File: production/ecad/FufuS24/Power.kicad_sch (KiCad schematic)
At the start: 57 parts, among them U4 TPS785, U5 PLMR38020FDDAR, U6 PLMR38020FDDAR, U7 PLMR38020FDDAR

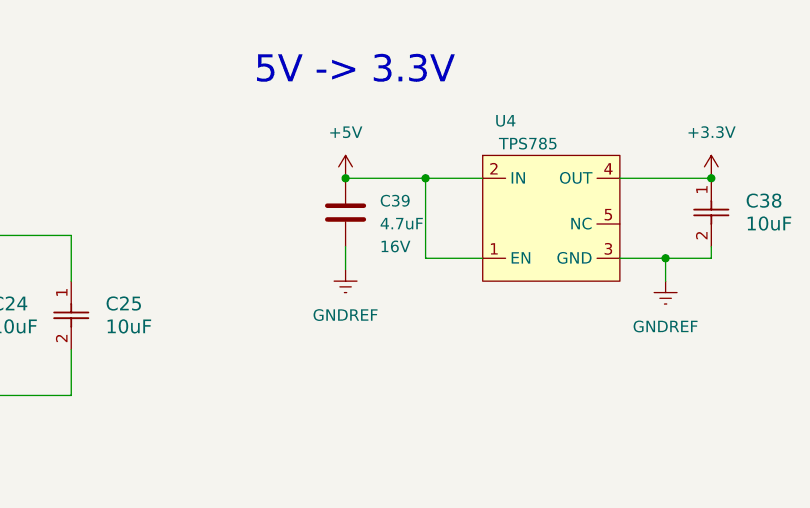
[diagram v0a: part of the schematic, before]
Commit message: updated some MPNs
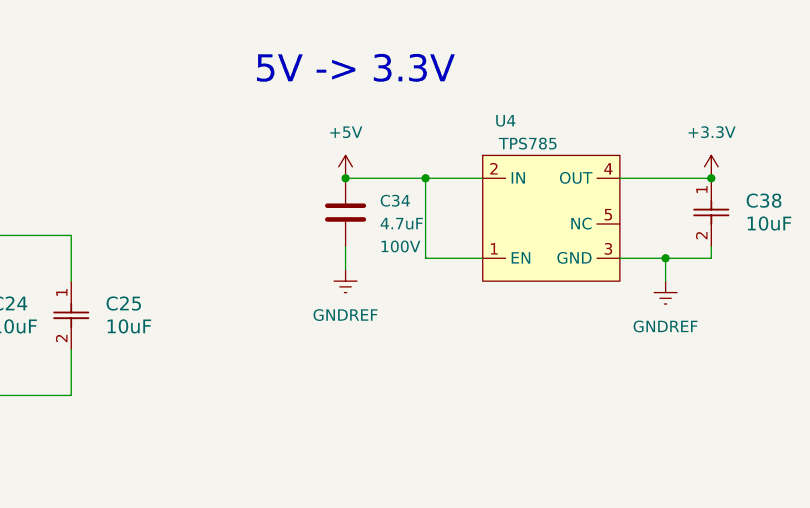
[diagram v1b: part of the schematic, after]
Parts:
- removed C39: 4.7uF, symbol Device:C
- added C34: 4.7uF, symbol Device:C
- C1, C27, C32: MPN (none) -> KAM32LR72A475KU
- C19, C20, C22, C26, C28, C33: MPN (none) -> CL21B104KCFNNNE
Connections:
- net +5V: now also C34.1
- net GNDREF: now also C34.2

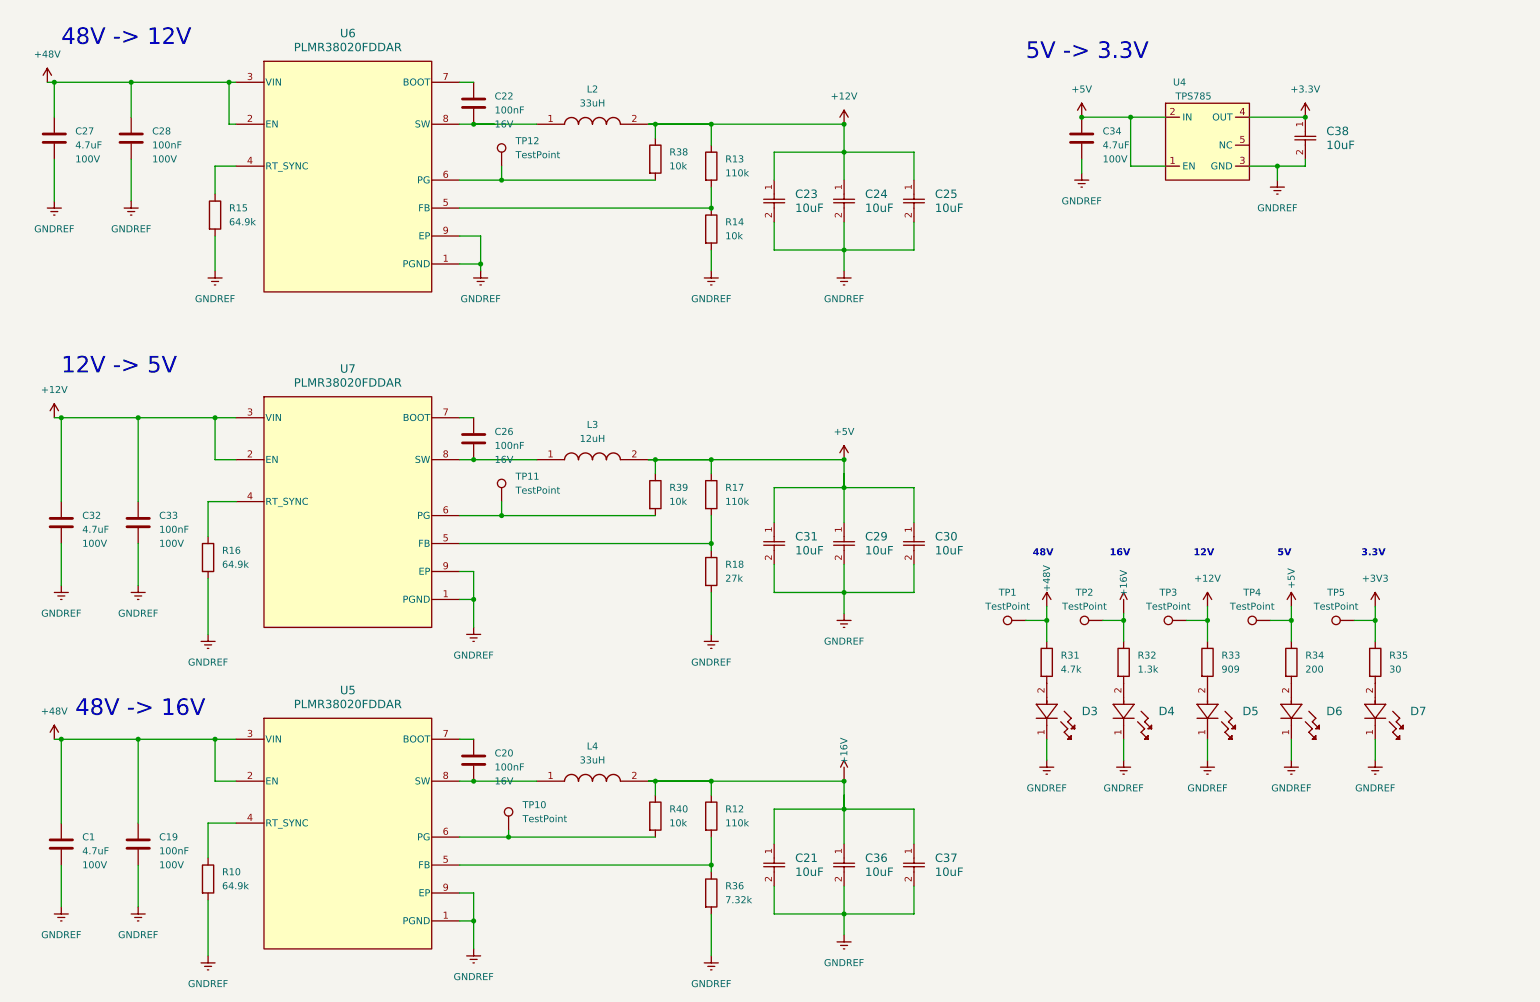
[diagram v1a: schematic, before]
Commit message: cleaned up schematic
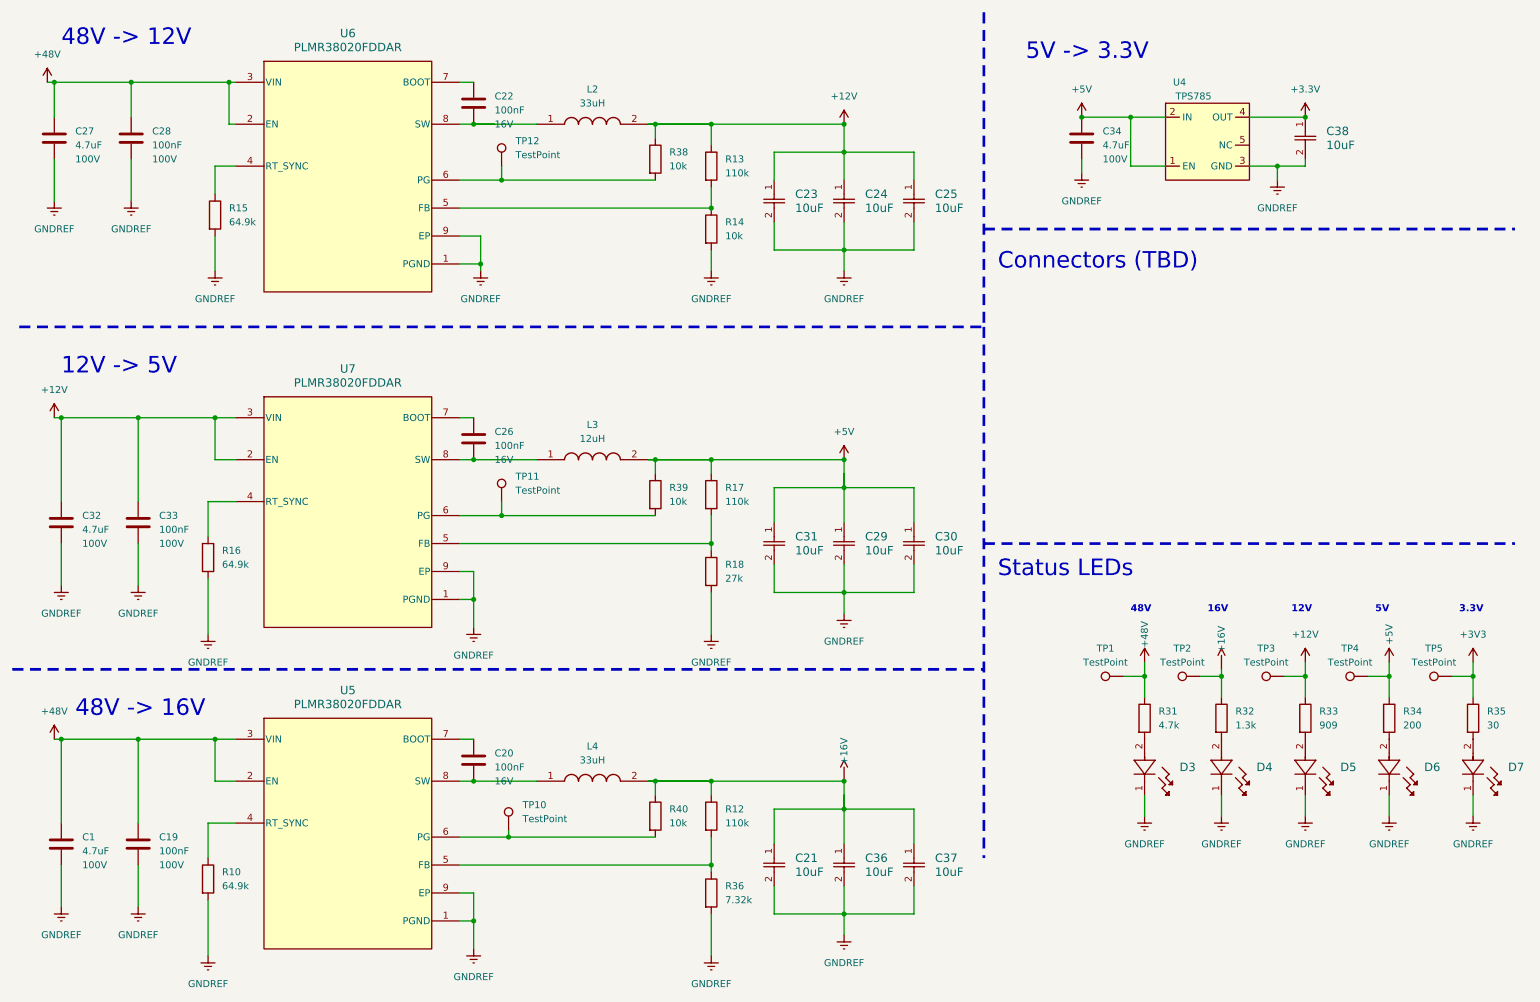
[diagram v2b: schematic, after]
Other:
- note added: "Connectors (TBD)"
- note added: "Status LEDs"
- moved on the sheet: D3, D4, D5, D6, D7, R31, R32, R33, R34, R35, TP1, TP2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

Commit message: Efan 6
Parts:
- C1, C19, C20, C21, C22, C23, C24, C25, C26, C27, C28, C29, C30, C31, C32, C33, C34, C36, C37, C38: footprint (none) -> footprints:CAPC2012X94N
- D3, D4, D5, D6, D7: footprint LED_GS75000_WRE -> (none)
- L3: footprint INDPM120120X800N -> (none)
- R10, R12, R13, R14, R15, R16, R17, R18, R31, R32, R33, R34, R35, R36, R38, R39, R40: footprint (none) -> footprints:RESC2012X60N
- TP1, TP10, TP11, TP12, TP2, TP3, TP4, TP5: footprint TestPoint:TestPoint_Pad_2.0x2.0mm -> footprints:TP_5014

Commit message: efan 7
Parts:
- D3, D4, D5, D6, D7: footprint (none) -> footprints:LED_GS75000_WRE
- L3: footprint (none) -> footprints:0805Inductor
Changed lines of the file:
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@@
       (effects (font (size 1.524 1.524)) (justify left) hide)
     )
-    (property "Footprint" "" (at 236.22 143.51 0)
+    (property "Footprint" "footprints:LED_GS75000_WRE" (at 236.22 143.51 0)
       (effects (font (size 1.27 1.27) italic) hide)
     )
@@
       (effects (font (size 1.524 1.524)) (justify left) hide)
     )
-    (property "Footprint" "" (at 266.7 143.51 0)
+    (property "Footprint" "footprints:LED_GS75000_WRE" (at 266.7 143.51 0)
       (effects (font (size 1.27 1.27) italic) hide)
     )
@@
       (effects (font (size 1.524 1.524)) (justify left) hide)
     )
-    (property "Footprint" "" (at 281.94 143.51 0)
+    (property "Footprint" "footprints:LED_GS75000_WRE" (at 281.94 143.51 0)
       (effects (font (size 1.27 1.27) italic) hide)
     )
@@
       (effects (font (size 1.524 1.524)) (justify left) hide)
     )
-    (property "Footprint" "" (at 251.46 143.51 0)
+    (property "Footprint" "footprints:LED_GS75000_WRE" (at 251.46 143.51 0)
       (effects (font (size 1.27 1.27) italic) hide)
     )
@@
       (effects (font (size 1.27 1.27)))
     )
-    (property "Footprint" "" (at 123.19 190.17 0)
+    (property "Footprint" "footprints:0805Inductor" (at 123.19 190.17 0)
       (effects (font (size 1.27 1.27)) (justify left top) hide)
     )
@@
       (effects (font (size 1.524 1.524)) (justify left) hide)
     )
-    (property "Footprint" "" (at 222.25 143.51 0)
-      (effects (font (size 1.27 1.27) italic) hide)
-    )
+    (property "Footprint" "footprints:LED_GS75000_WRE" (at 222.25 143.51 0)
+      (effects (font (size 1.27 1.27) italic) hide)
+    )

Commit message: efan finals before laying out
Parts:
- removed TP1, TP10, TP11, TP12, TP2, TP3, TP4, TP5: TestPoint, footprints:TP_5014, symbol Connector:TestPoint
- added J7: 691137710002, footprints:CONN2_710002_WRE, symbol 2024-03-03_19-32-21:691137710002
- added TP1, TP10, TP11, TP12, TP2, TP3, TP4, TP5: 5014, footprints:TP_5014, symbol 5014:5014
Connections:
- net +12V: now also TP3.TP
- net +16V: now also TP2.TP
- net +3V3: now also TP5.TP
- net +48V: now also J7.1, TP1.TP
- net +5V: now also TP4.TP
- net GNDREF: now also J7.2
- net at R39.2, U7.6 (PG): now also TP11.TP
- net at R40.2, U5.6 (PG): now also TP10.TP
- net at R38.2, U6.6 (PG): now also TP12.TP

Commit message: laying out
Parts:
- L3: footprint footprints:0805Inductor -> footprints:INDPM120120X800N
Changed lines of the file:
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@@
       (effects (font (size 1.27 1.27)))
     )
-    (property "Footprint" "footprints:0805Inductor" (at 123.19 190.17 0)
+    (property "Footprint" "footprints:INDPM120120X800N" (at 123.19 190.17 0)
       (effects (font (size 1.27 1.27)) (justify left top) hide)
     )
